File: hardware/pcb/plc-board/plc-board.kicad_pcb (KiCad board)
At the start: 2 copper layers, 100 x 80 mm, 62 parts, among them J1 MAINS_L_N, J2 ESP32_UART0_PROGRAMMING, J3 ST7580_JTAG_DEBUG, J4 TERMINAL_5V_IN, T1 750510231, U1 HLK-5M05, U2 ESP32-C3-MINI-1, U3 AMS1117-3.3, U4 ST7580, U5 MT3608, Y1 8MHz

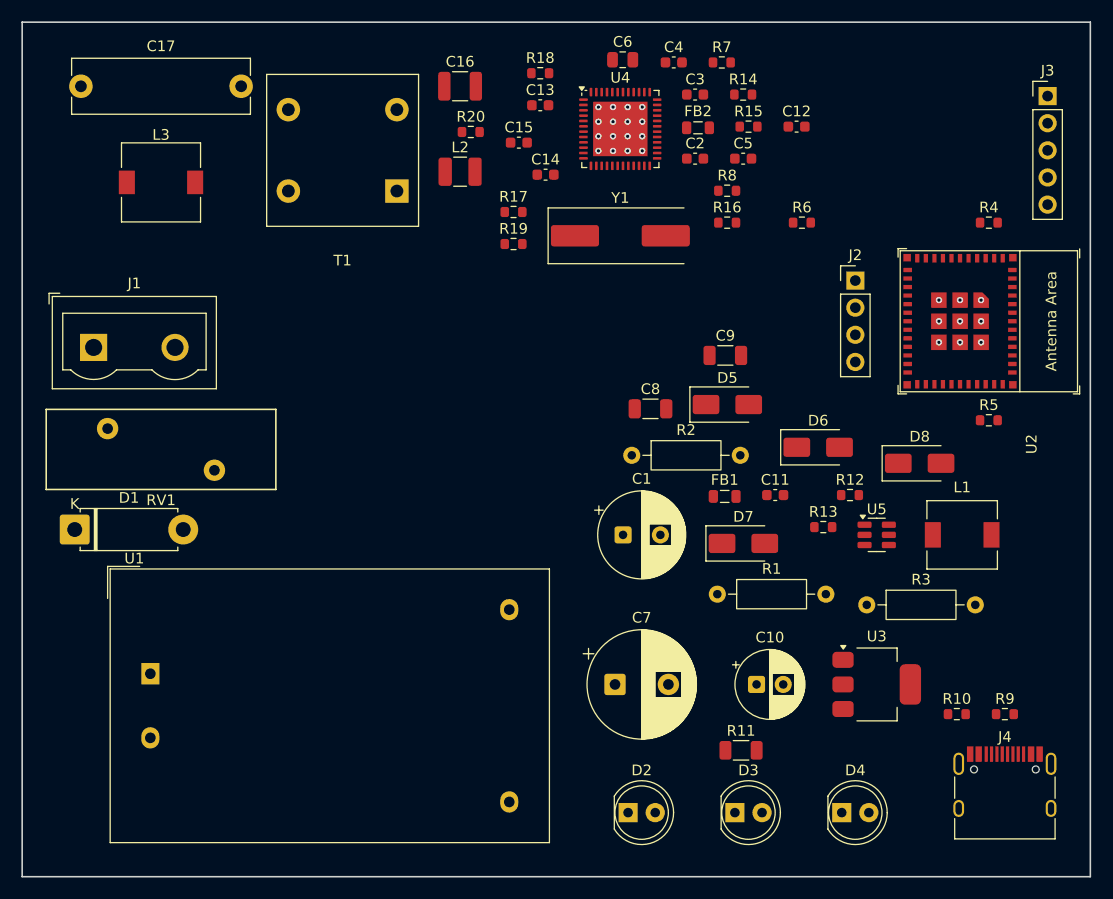
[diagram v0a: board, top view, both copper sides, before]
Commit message: hardware: make Board 1 four layers, and build the routing pipeline
Board 1 is a four-layer board, and not for signal density -- it could very
nearly be routed on two. It is four because of what has to be planed.

  L1  F.Cu    signals, all components
  L2  In1.Cu  GND plane   (4984 mm2, isolated side only)
  L3  In2.Cu  +5V plane   (4960 mm2, isolated side only)
  L4  B.Cu    signals

The ST7580 puts nine +5V pads on three edges of a 48-pin 0.5mm-pitch package.
Nothing passes between adjacent pads there -- a 0.2mm track with 0.2mm
clearance needs 0.6mm and the gap is 0.25mm -- so every pin escapes radially
and those nine have to find each other around the outside of eleven other
escapes. Four full two-layer routing runs failed on exactly that, never on
the same pad twice: (52.05,6.70), (59.45,11.25), (59.45,8.25), and twice on
the pin 3 / pin 48 pair that wraps the top-left corner. A fifth run with a
filled +5V island on F.Cu routed cleanly and was then broken by its own
ground pour, which chopped the island from 413mm2 to 109mm2 and stranded
eight connections. That net wants a plane, and on two layers both copper
layers are already spoken for by ground and the mains barrier.

The barrier goes through all four layers. An inner plane that crossed it
would bridge mains to SELV inside the laminate, where no inspection would
ever find it. Both keepout rule areas are on all four copper layers, both
planes stop at SELV_MIN, and that is measured rather than assumed: the filled
polygons start at exactly x = 33.98.

Also in this pass, before the layer change and independent of it: the
placement around U4 was wrong in a way that mattered electrically, not just
for routing. Support parts were placed at the centroid of the nets they join,
but a decoupling capacitor's job is to be beside its own pin. C6 (VCCA,
pin 17, bottom edge) and C4 (VDD_REG, pin 27, right edge) both sat above the
chip, in the corridor twelve top-edge pins have to escape through, leaving
0.7mm of clear widt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
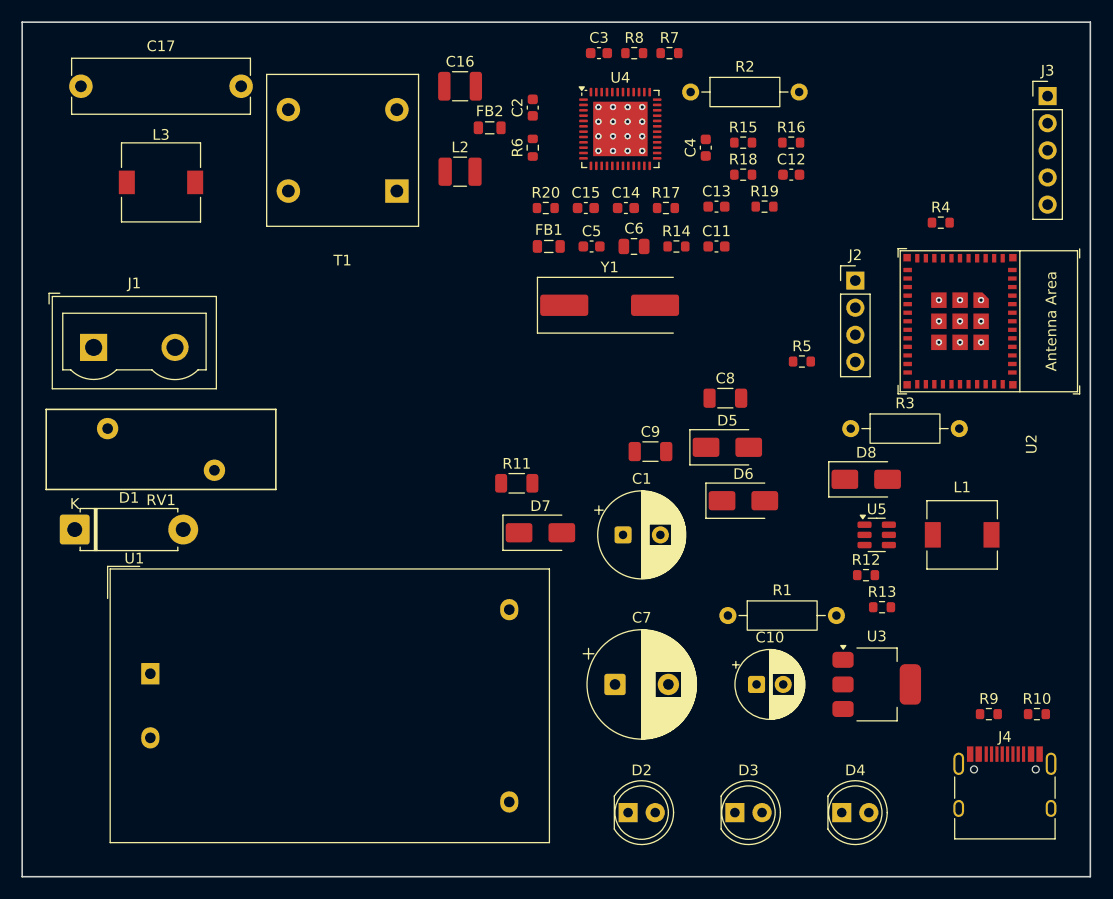
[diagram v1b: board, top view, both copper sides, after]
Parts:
- moved R2 34.5 mm to (62.6, 6.54)
- moved R11 32.6 mm to (46.3, 43.2)
- moved FB1 28.6 mm to (49.3, 21.0)
- moved R6 26.2 mm to (47.8, 11.8), turned to 90 degrees
- moved C11 23.9 mm to (65.0, 21.0)
- moved R19 23.8 mm to (69.5, 17.3)
- moved R18 21.2 mm to (67.5, 14.3)
- moved FB2 19.5 mm to (43.8, 9.89)
- moved C13 19.0 mm to (65.0, 17.3)
- moved D7 19.0 mm to (48.5, 47.8)
- moved R5 18.3 mm to (73.0, 31.8)
- moved C6 17.5 mm to (57.3, 21.0)
- moved R3 16.6 mm to (77.6, 38.0)
- moved C5 16.4 mm to (53.3, 21.0)
- moved C2 15.9 mm to (47.8, 8.00), turned to 90 degrees
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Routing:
- added copper zone on In2.Cu, net +5V
- added copper zone on In1.Cu, net GND
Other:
- copper layers 2 -> 4

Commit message: hardware: a routing pass on Board 1, and six defects it found
Routing does not finish. Every run still ends one connection short. What the
pass found is worth more than the routing would have been: six separate
defects stood between this board and a routed one, and each was invisible
until the router hit it.

The QFN's power pins had no fanout. The ST7580 puts nine +5V pads on three
edges of a 48-pin 0.5mm-pitch package; nothing passes between adjacent pads
there, so each escapes radially and the router then has to bring nine radial
escapes back together around the outside of eleven others. Every run this
project had made died on that -- with planes declared up front it was the
top-left corner pair and the right edge, with planes deferred it was the
right edge three times out of three. add_power_fanout() now gives each power
pad a 1.6mm stub and a via at build time, which is what a person does by hand
on a QFN and what no autorouter does for itself.

The pour ran after the repair, so those fanout vias were islands. Planes are
what connect them; until the copper is poured they are isolated points and
the repair router was being asked to tie them together -- the exact problem
the fanout removes. route.sh now pours before repairing. This is not the
ordering the Main Board warns about: there the danger is pouring before
*routing*, which makes the autorouter treat GND as already done. With the two
changes together, +5V stopped being a holdout at all.

The repair router ignored netclasses. It laid 0.2mm track at 0.2mm clearance
into the Mains class, which is 1.0mm at 2.5mm -- on the mains side not a style
question but the live-to-neutral spacing. Seven clearance errors in one run,
every one on /AC_L, /AC_N or /PLC_LINE, all laid by the step meant to be
finishing the job. It now reads the rules from the same table build_pcb.py
writes into the project file; KiCad 9's Python binding returns GetNetClass()
as a bare object with no accessors, so importing the source of truth is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
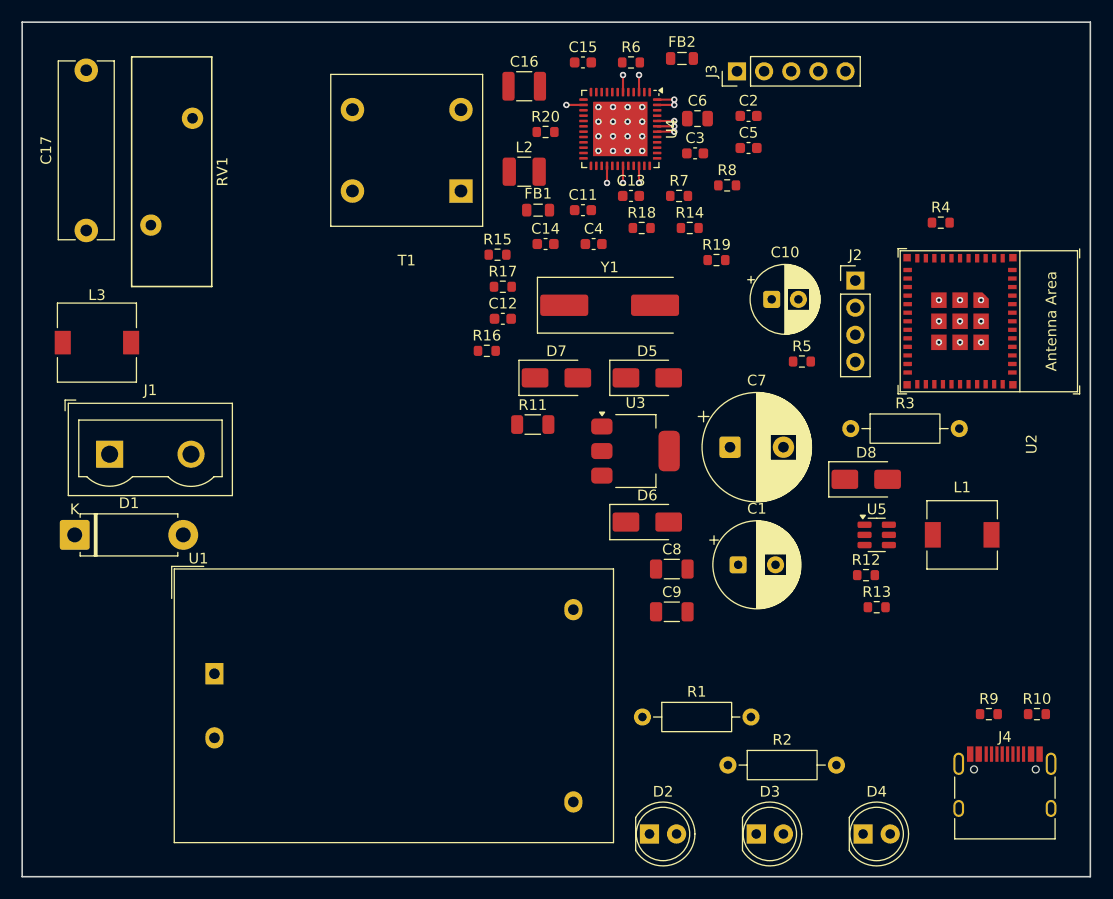
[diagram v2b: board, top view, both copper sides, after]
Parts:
- moved R2 63.1 mm to (66.1, 69.5)
- moved C10 36.1 mm to (70.2, 25.9)
- moved R16 34.5 mm to (43.5, 30.8)
- moved U3 31.4 mm to (57.4, 40.1)
- moved C12 30.2 mm to (45.0, 27.8)
- moved J3 29.2 mm to (66.9, 4.60), turned to 90 degrees
- moved R15 25.3 mm to (44.5, 21.8)
- moved C7 24.7 mm to (66.3, 39.8)
- moved C2 20.2 mm to (68.0, 8.78), turned to 0 degrees
- moved RV1 19.5 mm to (12.1, 19.0), turned to 90 degrees
- moved FB2 19.1 mm to (61.8, 3.40)
- moved C5 17.3 mm to (68.0, 11.8)
- moved R17 17.0 mm to (45.0, 24.8)
- moved C8 16.8 mm to (60.8, 51.2)
- moved L3 16.2 mm to (7.00, 30.0)
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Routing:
- net +5V: track 0.00 -> 14.4 mm, vias 0 -> 9
- net GND: track 0.00 -> 3.20 mm, vias 9 -> 11
- removed copper zone on In2.Cu, net +5V
- removed copper zone on In1.Cu, net GND

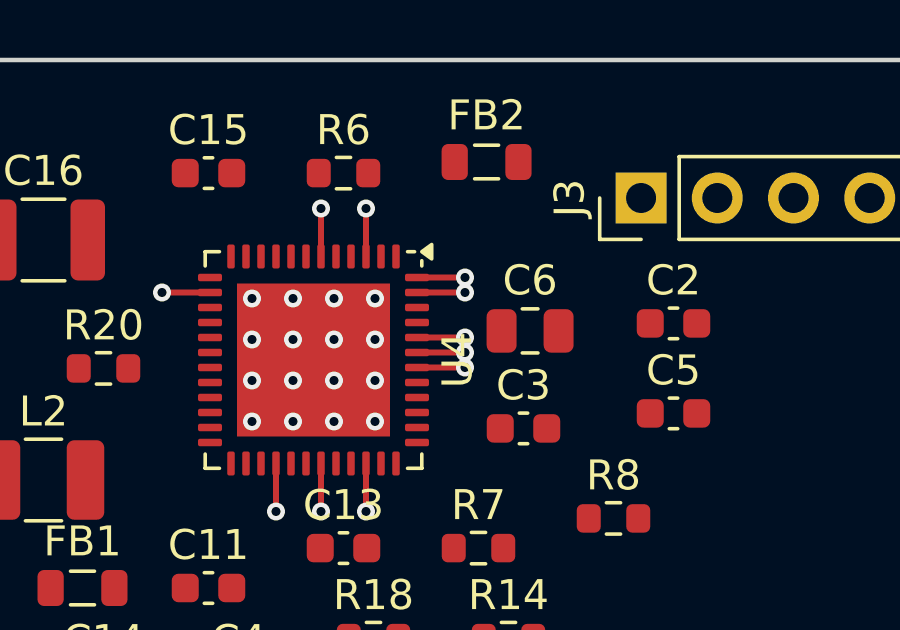
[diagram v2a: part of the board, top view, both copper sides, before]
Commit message: hardware: make the stackup a rule, and find that DRC had no minimums
The Main Board's stackup -- 1.6mm FR-4, two layers, 1oz copper -- had been
stated in its README and nowhere else, with the IPC-2221 trace-width table
depending on the copper weight. Closing that item turned up something worse
than an undocumented assumption.

KiCad's manufacturing minimums default to zero, and nothing had ever set
them. Both boards carried m_TrackMinWidth = 0.0 and m_MinClearance = 0.0
through every DRC run this project has reported. Every "0 violations" was
measured against no process limit at all: a 0.05mm trace, a via with no
annular ring, two holes touching -- all would have passed.

STACKUP in each board's build_pcb.py now writes the constraints into the
board's own design settings:

  1.6mm FR-4          0.2mm minimum track      0.6mm vias
  Board 2: 2 layers   0.2mm minimum clearance  0.3mm drills
  Board 1: 4 layers   0.15mm annular ring      0.25mm hole-to-hole

The values are what the boards already use, promoted from convention to rule,
so DRC catches anything that drifts below what the design was drawn to. The
Main Board's routed copper passes them unchanged -- 0 violations, 0
unconnected, exactly as before. That is the point: the rules describe the
board, they do not reshape it. It was applied to the routed board in place
rather than by regenerating, since re-routing would have thrown away a clean
result to no purpose.

On Board 1 the new rules caught a real defect immediately. The power fanout
sends each of U4's power pads 1.6mm straight out, and those pads are on a
0.5mm pitch -- so their vias landed on a 0.5mm pitch too, which with a 0.3mm
drill is 0.2mm hole-to-hole against the 0.25mm rule. Three pairs. The fanout
now checks hole spacing and steps a crowded neighbour further out; one pad of
eleven no longer gets a via and is left to the router, which is the right
trade.

Board 1's inner copper is lighter than its outer on a standard 4-layer stack.
That does not aff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
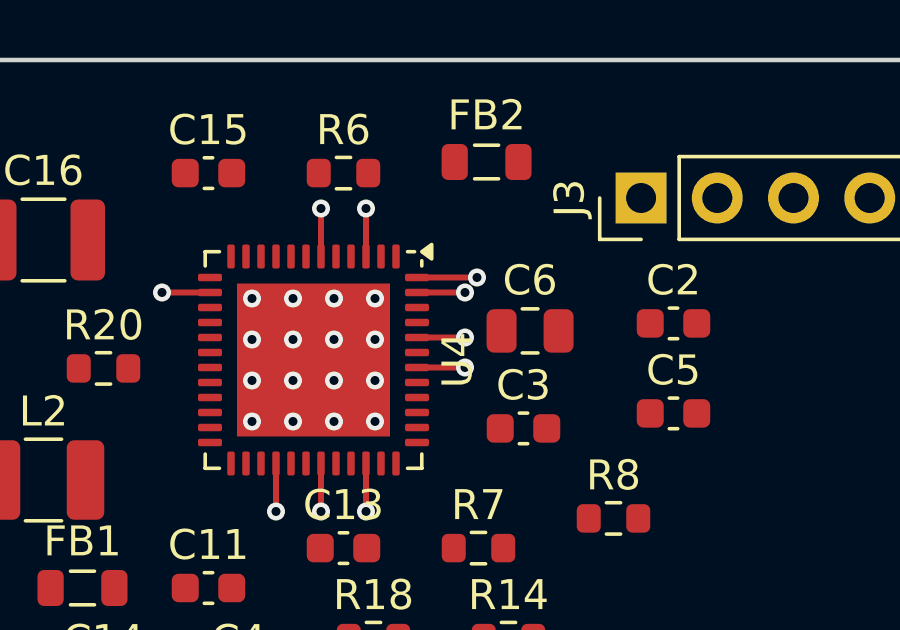
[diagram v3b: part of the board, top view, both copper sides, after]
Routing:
- net +5V: track 14.4 -> 13.2 mm, vias 9 -> 8
